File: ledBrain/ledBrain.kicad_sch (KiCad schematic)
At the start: 28 parts, among them CN1 XT30PW-M, SW1 K2-1112SW-A4SW-04, SW2 K2-1112SW-A4SW-04, SW3 K2-1112SW-A4SW-04, U1 QuinLED-ESP32, U2 MT30-F, U3 CH224A, U4 LM2940S-5.0, U6 SN74AHCT32QPWRQ1

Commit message: add layout
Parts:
- removed C15: 1uF, Capacitor_SMD:C_0603_1608Metric_Pad1.08x0.95mm_HandSolder, symbol Device:C
- removed C16: 0.1uF, Capacitor_SMD:C_0603_1608Metric_Pad1.08x0.95mm_HandSolder, symbol Device:C
- removed JP1: SolderJumper_2_Bridged, Jumper:SolderJumper-2_P1.3mm_Bridged_RoundedPad1.0x1.5mm, symbol Jumper:SolderJumper_2_Bridged
- removed MIC1: MP34DT05TR-A, easyeda2kicad:MIC-SMD_5P-L3.0-W4.0-P0.85-BL, symbol easyeda2kicad:MP34DT05TR-A
- removed R9: 10k, Resistor_SMD:R_0603_1608Metric_Pad0.98x0.95mm_HandSolder, symbol Device:R
- removed SW1: K2-1112SW-A4SW-04, easyeda2kicad:KEY-TH_K2-1112SW-AXXW-XX, symbol easyeda2kicad:K2-1112SW-A4SW-04
- removed U6: SN74AHCT32QPWRQ1, footprint:TSSOP-14_L5.0-W4.4-P0.65-LS6.5-BL, symbol GLOWINGKITTYPARTS:SN74AHCT32QPWRQ1
- added C8: 1uF, Capacitor_SMD:C_0603_1608Metric_Pad1.08x0.95mm_HandSolder, symbol Device:C
- added C9: 0.1uF, Capacitor_SMD:C_0603_1608Metric_Pad1.08x0.95mm_HandSolder, symbol Device:C
- added JP2: SolderJumper_2_Bridged, Jumper:SolderJumper-2_P1.3mm_Bridged_RoundedPad1.0x1.5mm, symbol Jumper:SolderJumper_2_Bridged
- added MIC2: MSM261DGT003, easyeda2kicad:MIC-SMD_6P-L4.0-W2.0_LMD4020T261-OC3, symbol easyeda2kicad:MSM261DGT003
- added U5: SN74AHCT32QPWRQ1, easyeda2kicad:TSSOP-14_L5.0-W4.4-P0.65-LS6.5-BL, symbol easyeda2kicad:SN74AHCT32QPWRQ1
- renumbered Rset to Rset1
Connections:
- net +12V: now also U2.3
- net +3.3V: now also JP2.1 (A)
- net +5V: now also U5.14 (VCC)
- net GND: now also CN1.3, CN1.4, SW2.3, SW2.4, SW3.3, SW3.4, U2.1, C8.1, C9.1, MIC2.2 (GND), MIC2.5 (GND), MIC2.6 (L/R), U5.10 (3B), U5.11 (4Y), U5.12 (4A), U5.13 (4B), U5.2 (1B), U5.4 (2A), U5.5 (2B), U5.6 (2Y), U5.7 (GND), U5.8 (3Y), U5.9 (3A)
- net IO12/MIC CLK: now also MIC2.4 (CLK)
- net IO16/LED1: now also U5.1 (1A)
- net IO32/MIC DATA: now also MIC2.3 (DATA)
- net LED DATA OUT: now also U2.2
- net at R1.2: now also U5.3 (1Y)
- new net: C8.2, C9.2, JP2.2 (B), MIC2.1 (VDD)
- no-connect marks 5 -> 3
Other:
- moved on the sheet: C4, C5, C6, C7, U2, U4

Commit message: add some more
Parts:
- removed U4: LM2940S-5.0, easyeda2kicad:SOT-223-3_L6.5-W3.4-P2.30-LS7.0-BR, symbol easyeda2kicad:LM2940S-5.0
- added C10, C16, Cboot: 1uF, Capacitor_SMD:C_0805_2012Metric_Pad1.18x1.45mm_HandSolder, symbol Device:C
- added C11, C15: 100nF, Capacitor_SMD:C_0805_2012Metric_Pad1.18x1.45mm_HandSolder, symbol Device:C
- added C12, C13, C14, Cin, Cout: 10uF, Capacitor_SMD:C_0805_2012Metric_Pad1.18x1.45mm_HandSolder, symbol Device:C
- added CN2, CN3, CN4: TR54130180-1500, easyeda2kicad:CONN-TH_TR54130180-1500, symbol easyeda2kicad:TR54130180-1500
- added CN5: PJ-328A0-B, easyeda2kicad:AUDIO-TH_PJ-328A0-B, symbol easyeda2kicad:PJ-328A0-B
- added D2: D, symbol Device:D
- added JP1, JP3: SolderJumper_2_Bridged, Jumper:SolderJumper-2_P1.3mm_Bridged_RoundedPad1.0x1.5mm, symbol Jumper:SolderJumper_2_Bridged
- added L1: 10uH, symbol Device:L
- added R10, R11, R12, R7, R8, R9: 10k, Resistor_SMD:R_0603_1608Metric_Pad0.98x0.95mm_HandSolder, symbol Device:R
- added R13, R16, R5, R6: 100R, Resistor_SMD:R_0603_1608Metric_Pad0.98x0.95mm_HandSolder, symbol Device:R
- added R2: 3.3M, Resistor_SMD:R_0603_1608Metric_Pad0.98x0.95mm_HandSolder, symbol Device:R
- added R3: 5.1k, Resistor_SMD:R_0603_1608Metric_Pad0.98x0.95mm_HandSolder, symbol Device:R
- added R4: 1k, Resistor_SMD:R_0603_1608Metric_Pad0.98x0.95mm_HandSolder, symbol Device:R
- added U4: ME3116, easyeda2kicad:SOT-23-6_L2.9-W1.6-P0.95-LS2.8-BL, symbol easyeda2kicad:ME3116
- added U6: PCM1808PWR, easyeda2kicad:TSSOP-14_L5.0-W4.4-P0.65-LS6.4-BL, symbol easyeda2kicad:PCM1808PWR
- C6: value 10uF -> 47pF
- C7: value 10uF -> 100nF
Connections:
- net +3.3V: now also JP1.1 (A), R7.1, R8.1, R9.1
- net +5V: now also C6.1, Cout.2, JP3.1 (A), L1.2, R3.1; no longer C7.2
- net GND: now also C7.2, C11.2, C12.2, C13.2, C14.1, C15.1, CN4.1, CN4.2, CN4.3, CN4.4, Cin.2, Cout.1, D2.2 (A), R10.2, R11.2, R12.2, R4.2, U4.2 (GND), U6.2 (AGND), U6.5 (DGND); no longer C6.2, C7.1
- net LED DATA OUT: now also CN3.1, CN3.2, CN3.3, CN3.4
- net SD: now reaches U1.18 (IO13)
- net SD: now also R13.1
- net MCLK: now reaches U1.34 (IO_0)
- net MCLK: now also R5.2
- net WS: now reaches U1.4 (IO35)
- net WS: now also R6.2
- net SCK: now reaches U1.7 (IO14)
- net SCK: now also R16.1
- net +12V renamed VDD
- net VDD: now also CN2.1, CN2.2, CN2.3, CN2.4, Cin.1, R2.1, U4.5 (IN); no longer C6.1
- new net: C6.2, R3.2, R4.1, U4.3 (FB)
- new net: C12.1, C7.1, U6.1 (VREF)
- new net: R12.1, R9.2, U6.10 (MD0)
- new net: R11.1, R8.2, U6.11 (MD1)
- new net: R10.1, R7.2, U6.12 (FMT)
- new net: C16.2, U6.13 (VINL)
- new net: C10.2, U6.14 (VINR)
- new net: C11.1, C13.1, JP3.2 (B), U6.3 (VCC)
- new net: C14.2, C15.2, JP1.2 (B), U6.4 (VDD)
- new net: R5.1, U6.6 (SCKI)
- new net: R6.1, U6.7 (LRCK)
- new net: R16.2, U6.8 (BCK)
- new net: R13.2, U6.9 (DOUT)
- new net: Cboot.1, U4.1 (BS)
- new net: R2.2, U4.4 (EN)
- new net: Cboot.2, D2.1 (K), L1.1, U4.6 (SW)
- new net AUXIN_L: C16.1
- new net AUXIN_R: C10.1
- no-connect marks 3 -> 13
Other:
- note added: "5V Buck"
- note added: "I2C Digital Line-In"
- note added: "MCLK (Master Clock) signal, can only be generated by the ESP32 on GPIOs 0, 1 or 3"
- note added: "Pins used for the ethernet extension board (Do not use those)"
- note added: "USB-C PD Select Voltage"
- moved on the sheet: C3, C4, C5, C8, C9, D1, JP2, MIC2, Rset1, U2, U3, USB1

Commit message: update
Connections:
- net AUXIN_L: now also CN5.3
- net AUXIN_R: now also CN5.2
- net GND: now also CN5.1
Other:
- note added: "Line-In"
- note added: "the footprint is broken. I needed to put the connector on the wrong side"
- note removed: "check right pinout"
- moved on the sheet: C4, C5, C6, C8, C9, CN1, CN5, Cboot, Cin, Cout, D2, DC1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

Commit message: update
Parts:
- removed C8: 1uF, Capacitor_SMD:C_0603_1608Metric_Pad1.08x0.95mm_HandSolder, symbol Device:C
- removed C9: 0.1uF, Capacitor_SMD:C_0603_1608Metric_Pad1.08x0.95mm_HandSolder, symbol Device:C
- removed CN2, CN3, CN4: TR54130180-1500, easyeda2kicad:CONN-TH_TR54130180-1500, symbol easyeda2kicad:TR54130180-1500
- removed JP2: SolderJumper_2_Bridged, Jumper:SolderJumper-2_P1.3mm_Bridged_RoundedPad1.0x1.5mm, symbol Jumper:SolderJumper_2_Bridged
- removed MIC2: MSM261DGT003, easyeda2kicad:MIC-SMD_6P-L4.0-W2.0_LMD4020T261-OC3, symbol easyeda2kicad:MSM261DGT003
- removed SW3: K2-1112SW-A4SW-04, easyeda2kicad:KEY-TH_K2-1112SW-AXXW-XX, symbol easyeda2kicad:K2-1112SW-A4SW-04
- removed U2: MT30-F, easyeda2kicad:CONN-TH_MT30-M, symbol easyeda2kicad:MT30-F
- added C17, C18: 10uF, Capacitor_SMD:C_0805_2012Metric_Pad1.18x1.45mm_HandSolder, symbol Device:C
- added C19: 100nF, Capacitor_SMD:C_0805_2012Metric_Pad1.18x1.45mm_HandSolder, symbol Device:C
- added C20: 15pF, Capacitor_SMD:C_0805_2012Metric_Pad1.18x1.45mm_HandSolder, symbol Device:C
- added C21, C22, C29, C30: 1uF, Capacitor_SMD:C_0805_2012Metric_Pad1.18x1.45mm_HandSolder, symbol Device:C
- added C23, C24, C25, C27, C28: 0.1uF, Capacitor_SMD:C_0805_2012Metric_Pad1.18x1.45mm_HandSolder, symbol Device:C
- added C26: 2.2uF, Capacitor_SMD:C_0805_2012Metric_Pad1.18x1.45mm_HandSolder, symbol Device:C
- added OSC1: OT2EL4C4JI-111OLP-12.288M, easyeda2kicad:OSC-SMD_4P-L3.2-W2.5-BL, symbol easyeda2kicad:OT2EL4C4JI-111OLP-12.288M
- added R17, R18: 10k, Resistor_SMD:R_0603_1608Metric_Pad0.98x0.95mm_HandSolder, symbol Device:R
- added R19: 150k or NC, Resistor_SMD:R_0603_1608Metric_Pad0.98x0.95mm_HandSolder, symbol Device:R
- added R20: 100k or 0R, Resistor_SMD:R_0603_1608Metric_Pad0.98x0.95mm_HandSolder, symbol Device:R
- added SW1: EC11E09244BS, easyeda2kicad:SW-TH_EC11XXXXXXXX, symbol easyeda2kicad:EC11E09244BS
- added TP1: VDD, TestPoint:TestPoint_Plated_Hole_D3.0mm, symbol Connector:TestPoint
- added TP2: GND, TestPoint:TestPoint_Plated_Hole_D3.0mm, symbol Connector:TestPoint
- added U10: HS96L03W2C03, easyeda2kicad:OLED-TH_L27.8-W27.2-P2.54_C9900033791, symbol easyeda2kicad:HS96L03W2C03
- added U11: MAX9814ETD+T, easyeda2kicad:TDFN-14_L3.0-W3.0-P0.40-BL-EP, symbol easyeda2kicad:MAX9814ETD+T
- added U12: NA-FFA381-A10-1, easyeda2kicad:MIC-SMD_4P-L2.8-W1.9_NA-FFA381-A10-1, symbol easyeda2kicad:NA-FFA381-A10-1
- added U7, U8, U9: T34069, easyeda2kicad:XFCN_PKT-TH_4P-T34069, symbol easyeda2kicad:T34069
- C10, C16: value 1uF -> 10uF
- R7, R8, R9: now not fitted
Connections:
- net +3.3V: now also R15.1, C17.1, C18.1, C19.1, C30.1, OSC1.1 (Tri-state), OSC1.4 (VDD), R17.1, R18.1, U10.2 (VCC), U11.10 (GAIN), U11.2 (~{SHDN}), U11.5 (VDD)
- net +5V: no longer R15.2
- net AUXIN_L: now also CN5.2; no longer CN5.3
- net AUXIN_R: now also CN5.3; no longer CN5.2
- net GND: now also C17.2, C18.2, C19.2, C20.1, C21.2, C23.1, C25.2, C26.2, C27.2, C28.2, C29.2, C30.2, OSC1.2 (GND), R20.2, SW1.6, SW1.7, SW1.C, SW1.D, TP2.1, U10.1 (GND), U11.15 (EP), U11.7 (GND), U11.9 (A/R), U12.2 (GND), U12.3 (GND), U7.1, U7.2, U7.3, U7.4
- net LED DATA OUT: now also U8.1, U8.2, U8.3, U8.4
- net VDD: now also TP1.1, U9.1, U9.2, U9.3, U9.4
- net MIC AMP OUT: now reaches CN5.10
- net MIC AMP OUT: now also CN5.11, C22.2
- net MAINBUTTON: now reaches U1.27 (IO15)
- net MAINBUTTON: now also R14.1, SW2.1
- net ROTARY BUTTON: now reaches U1.3 (S_VN)
- net ROTARY BUTTON: now also C25.1, R18.2, SW1.E
- net DISPLAY SDA: now reaches U1.33 (IO_4)
- net DISPLAY SDA: now also U10.4 (SDA)
- net IO12/MIC CLK: no longer names the net of U1.32 (IO12)
- net IO16/LED1 renamed LED1
- net IO32/MIC DATA renamed DISPLAY SCL
- net DISPLAY SCL: now also U10.3 (SCL)
- removed net IO33/MAINBUTTON: R14.1, SW2.1, U1.5 (IO33)
- net IO34/SECOND BUTTON renamed ROTARY CLK
- net ROTARY CLK: now also R15.2, C28.1, SW1.A; no longer R15.1
- net MCLK: no longer names the net of U1.34 (IO_0)
- net MCLK: no longer R5.2
- net SCK renamed AUDIO SCK
- net SD renamed AUDIO SD
- net WS renamed AUDIO WS
- new net: C24.1, U12.4 (Output)
- new net: C21.1, U11.1 (CT)
- new net: C22.1, U11.6 (MICOUT)
- new net: R19.2, R20.1, U11.14 (TH)
- new net: C26.1, U11.3 (CG)
- new net: C29.1, U11.12 (BIAS)
- new net AUDIO MCLK: C20.2, OSC1.3 (OUT), R5.2
- new net MIC OUT: C24.2, U11.8 (MICIN)
- new net MICBIAS: C23.2, R19.1, U11.13 (MICBIAS), U12.1 (VDD)
- new net ROTARY DT: C27.1, R17.2, SW1.B, U1.5 (IO33)
- no-connect marks 13 -> 15
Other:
- note added: "Active Oscillator"
- note added: "Audio In"
- note added: "Audio to I2C Chip"
- note added: "Button"
- note added: "CT: 1µF to 2.2µF capacitor. This determines how fast the "auto-volume" reacts. GAIN: maximum amplification. GND: 50dB VCC: 40dB Floating: 60dB gain"
- note added: "Heat dissipation"
- note added: "Line-In Jack with passthrough"
- note added: "MCLK (Master Clock) signal, can only be generated by the ESP32 on GPIOs 0, 1 or 3. But the ESP32 cannot generate two different frequencies (50MHz for Ethernet and ~12MHz for Audio) from the APLL simultaneously -> Active Crystal Oscillator"
- note added: "Mic"
- note added: "OLED Display"
- note added: "Plated Holes for potential PoE later"
- note added: "Pre-amp"
- note added: "Rotary Encoder"
- note added: "TH sets when the "Auto-Volume" (AGC) kicks in. Connect it to GND for the lowest threshold. Use a resistor divider between VDD and GND for better control"
- note removed: "Buttons"
- note removed: "I2C Digital Line-In"
- note removed: "Line-In"
- note removed: "MCLK (Master Clock) signal, can only be generated by the ESP32 on GPIOs 0, 1 or 3"
- note removed: "PDM Microphone"
- note removed: "the footprint is broken. I needed to put the connector on the wrong side"
- moved on the sheet: C1, C10, C11, C12, C13, C14, C15, C16, C3, C4, C5, C6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

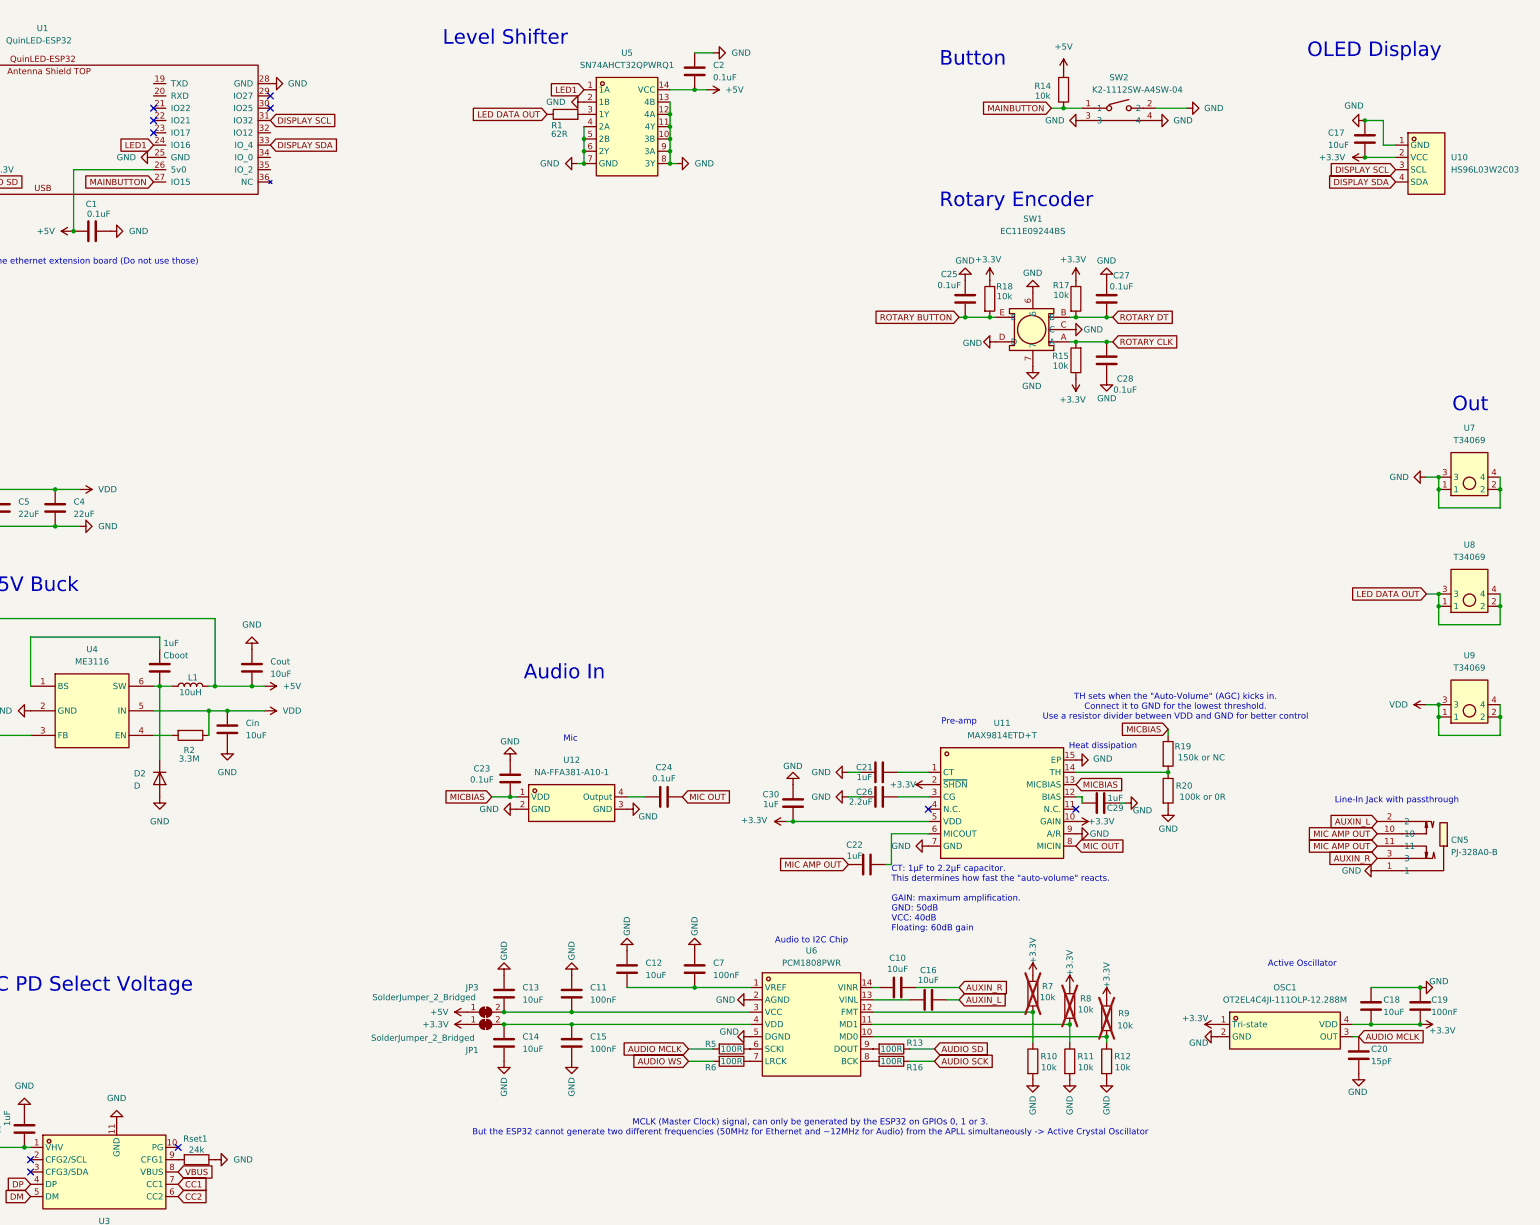
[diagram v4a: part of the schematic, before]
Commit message: new routing for ledbrain
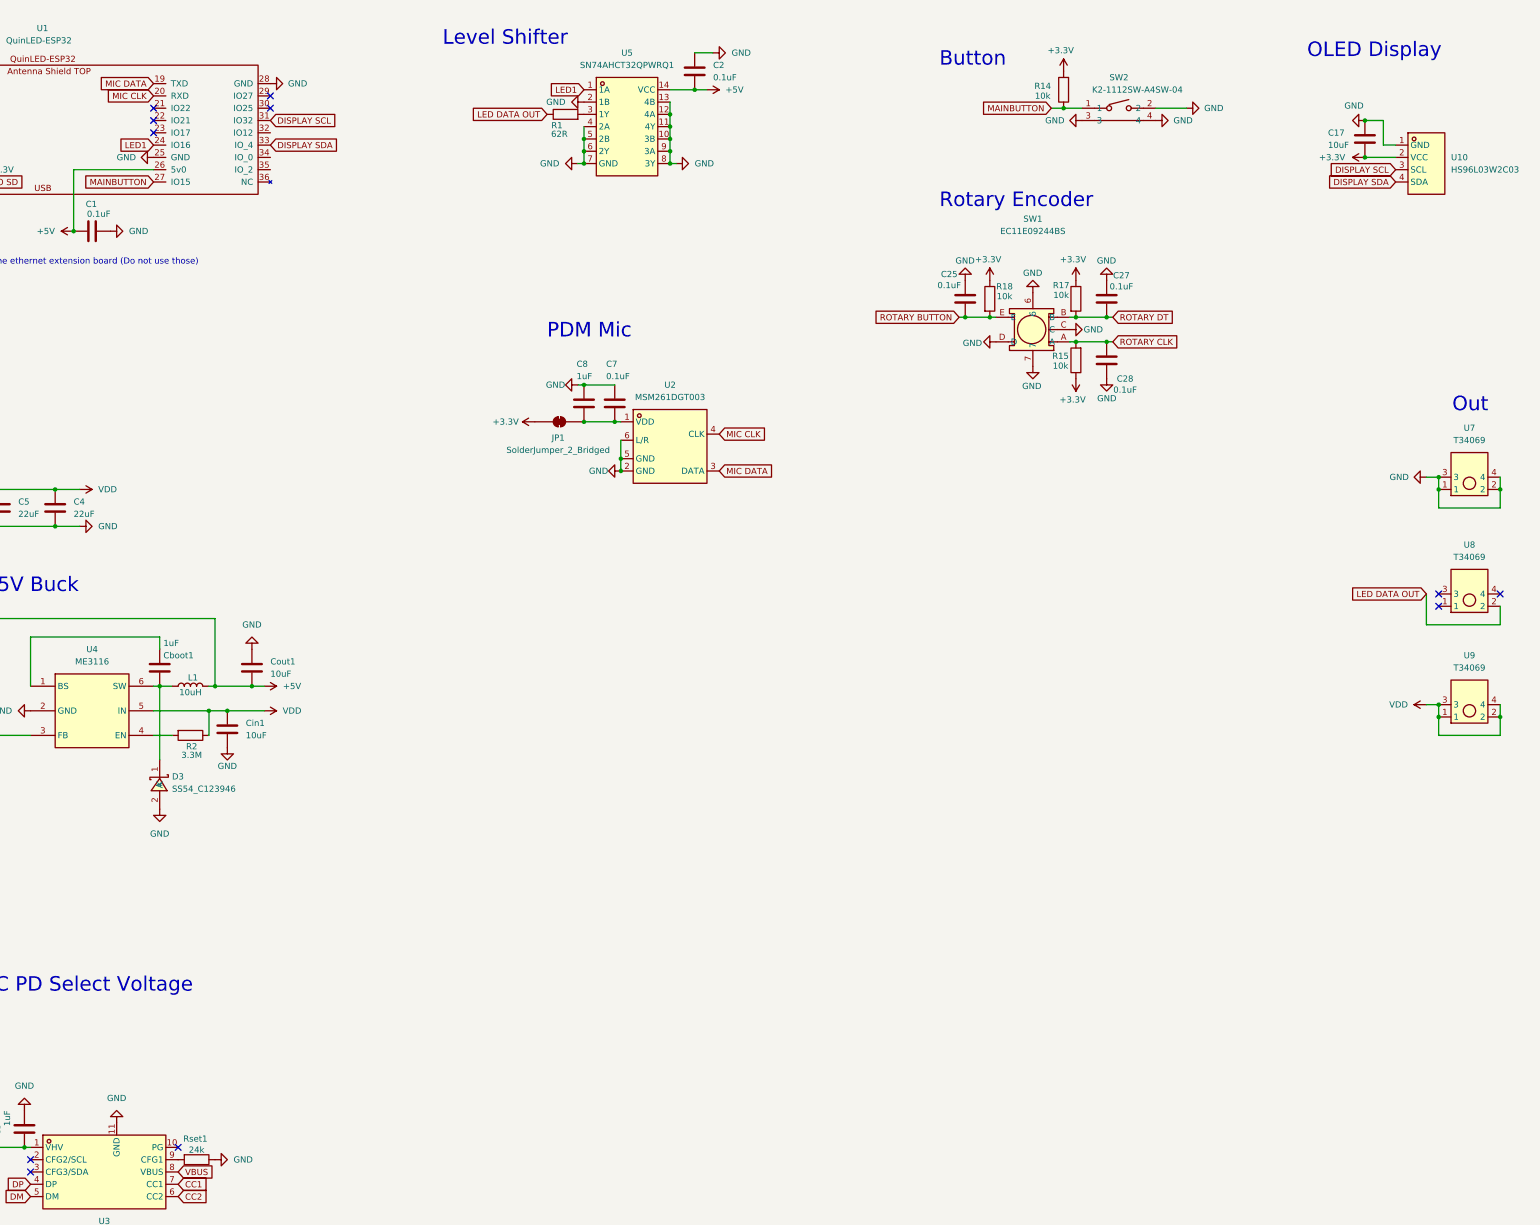
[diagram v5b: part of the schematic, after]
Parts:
- removed C10, C12, C13, C14, C16, C18: 10uF, Capacitor_SMD:C_0805_2012Metric_Pad1.18x1.45mm_HandSolder, symbol Device:C
- removed C11, C15, C19: 100nF, Capacitor_SMD:C_0805_2012Metric_Pad1.18x1.45mm_HandSolder, symbol Device:C
- removed C20: 15pF, Capacitor_SMD:C_0805_2012Metric_Pad1.18x1.45mm_HandSolder, symbol Device:C
- removed C21, C22, C29, C30: 1uF, Capacitor_SMD:C_0805_2012Metric_Pad1.18x1.45mm_HandSolder, symbol Device:C
- removed C23, C24: 0.1uF, Capacitor_SMD:C_0805_2012Metric_Pad1.18x1.45mm_HandSolder, symbol Device:C
- removed C26: 2.2uF, Capacitor_SMD:C_0805_2012Metric_Pad1.18x1.45mm_HandSolder, symbol Device:C
- removed CN5: PJ-328A0-B, easyeda2kicad:AUDIO-TH_PJ-328A0-B, symbol easyeda2kicad:PJ-328A0-B
- removed D2: D, symbol Device:D
- removed JP3: SolderJumper_2_Bridged, Jumper:SolderJumper-2_P1.3mm_Bridged_RoundedPad1.0x1.5mm, symbol Jumper:SolderJumper_2_Bridged
- removed OSC1: OT2EL4C4JI-111OLP-12.288M, easyeda2kicad:OSC-SMD_4P-L3.2-W2.5-BL, symbol easyeda2kicad:OT2EL4C4JI-111OLP-12.288M
- removed R10, R11, R12, R7, R8, R9: 10k, Resistor_SMD:R_0603_1608Metric_Pad0.98x0.95mm_HandSolder, symbol Device:R
- removed R13, R16, R5, R6: 100R, Resistor_SMD:R_0603_1608Metric_Pad0.98x0.95mm_HandSolder, symbol Device:R
- removed R19: 150k or NC, Resistor_SMD:R_0603_1608Metric_Pad0.98x0.95mm_HandSolder, symbol Device:R
- removed R20: 100k or 0R, Resistor_SMD:R_0603_1608Metric_Pad0.98x0.95mm_HandSolder, symbol Device:R
- removed U11: MAX9814ETD+T, easyeda2kicad:TDFN-14_L3.0-W3.0-P0.40-BL-EP, symbol easyeda2kicad:MAX9814ETD+T
- removed U12: NA-FFA381-A10-1, easyeda2kicad:MIC-SMD_4P-L2.8-W1.9_NA-FFA381-A10-1, symbol easyeda2kicad:NA-FFA381-A10-1
- removed U6: PCM1808PWR, easyeda2kicad:TSSOP-14_L5.0-W4.4-P0.65-LS6.4-BL, symbol easyeda2kicad:PCM1808PWR
- added C8: 1uF, Capacitor_SMD:C_0603_1608Metric_Pad1.08x0.95mm_HandSolder, symbol Device:C
- added D3: SS54_C123946, easyeda2kicad:SMA_L4.4-W2.8-LS5.4-RD, symbol easyeda2kicad:SS54_C123946
- added U2: MSM261DGT003, easyeda2kicad:MIC-SMD_6P-L4.0-W2.0_LMD4020T261-OC3, symbol easyeda2kicad:MSM261DGT003
- C7: value 100nF -> 0.1uF; footprint Capacitor_SMD:C_0805_2012Metric_Pad1.18x1.45mm_HandSolder -> Capacitor_SMD:C_0603_1608Metric_Pad1.08x0.95mm_HandSolder
- JP1: now left out of the parts list
- L1: footprint (none) -> Inductor_SMD:L_APV_ANR4030
- TP1, TP2: footprint TestPoint:TestPoint_Plated_Hole_D3.0mm -> TestPoint:TestPoint_Plated_Hole_D2.0mm
- renumbered Cboot to Cboot1, Cin to Cin1, Cout to Cout1
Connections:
- net +3.3V: now also R14.2
- net +5V: no longer R14.2
- net GND: now also C7.1, C8.1, D3.2 (A), U2.2 (GND), U2.5 (GND), U2.6 (L/R); no longer C7.2
- net LED DATA OUT: no longer U8.1, U8.3, U8.4
- net at JP1.2 (B): now also C7.2, C8.2, U2.1 (VDD)
- net at Cboot1.2, L1.1, U4.6 (SW): now also D3.1 (K)
- net MIC DATA: now reaches U1.19 (TXD)
- net MIC DATA: now also U2.3 (DATA)
- net MIC CLK: now reaches U1.20 (RXD)
- net MIC CLK: now also U2.4 (CLK)
- no-connect marks 15 -> 16
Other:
- note added: "PDM Mic"
- note removed: "Active Oscillator"
- note removed: "Audio In"
- note removed: "Audio to I2C Chip"
- note removed: "CT: 1µF to 2.2µF capacitor. This determines how fast the "auto-volume" reacts. GAIN: maximum amplification. GND: 50dB VCC: 40dB Floating: 60dB gain"
- note removed: "Heat dissipation"
- note removed: "Line-In Jack with passthrough"
- note removed: "MCLK (Master Clock) signal, can only be generated by the ESP32 on GPIOs 0, 1 or 3. But the ESP32 cannot generate two different frequencies (50MHz for Ethernet and ~12MHz for Audio) from the APLL simultaneously -> Active Crystal Oscillator"
- note removed: "Mic"
- note removed: "Pre-amp"
- note removed: "TH sets when the "Auto-Volume" (AGC) kicks in. Connect it to GND for the lowest threshold. Use a resistor divider between VDD and GND for better control"
